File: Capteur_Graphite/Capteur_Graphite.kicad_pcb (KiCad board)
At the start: 2 copper layers, 68.6 x 53.3 mm, 25 parts, among them J1 Power, J2 Digital/PWM, J3 Analog, J4 Digital/PWM, U1 LTC1050ACN8_PBF, U2 MCP41050

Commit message: Clear PCB
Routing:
- net 13: track 111.3 -> 0.00 mm
- net +5: track 95.2 -> 0.26 mm
- net /SCL/A5: track 81.7 -> 0.00 mm
- net A1: track 41.1 -> 0.00 mm
- net R2: track 30.6 -> 0.00 mm
- net GND: track 20.9 -> 0.79 mm
- net Net-(U1-OUT): track 18.1 -> 0.14 mm
- net Net-(U1-+IN): track 17.0 -> 0.00 mm
- net A0: track 7.29 -> 0.00 mm
- net P2: track 5.45 -> 0.00 mm
- net Net-(Capteur1-cn): track 5.20 -> 0.00 mm

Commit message: Schematique propre
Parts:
- removed Encodeur: ~, Ma_Lib_Empreinte_Projet_Capteur:Rotatoire
- added U6: ~, Ma_Lib_Empreinte_Projet_Capteur:Rotatoire, F.Cu at (156.4, 53.5)
- C1, C2: footprint Capacitor_THT:C_Disc_D3.0mm_W1.6mm_P2.50mm -> Capacitor_THT:C_Disc_D5.0mm_W2.5mm_P5.00mm
- C3, C4: footprint Capacitor_THT:C_Rect_L4.6mm_W2.0mm_P2.50mm_MKS02_FKP02 -> Capacitor_THT:C_Rect_L7.0mm_W4.5mm_P5.00mm
- R1: footprint Resistor_THT:R_Axial_DIN0204_L3.6mm_D1.6mm_P7.62mm_Horizontal -> Resistor_THT:R_Axial_DIN0309_L9.0mm_D3.2mm_P5.08mm_Vertical
- R3, R5, R6: footprint Resistor_THT:R_Axial_DIN0204_L3.6mm_D1.6mm_P1.90mm_Vertical -> Resistor_THT:R_Axial_DIN0309_L9.0mm_D3.2mm_P5.08mm_Vertical

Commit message: Fin de séance du 13 mars
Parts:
- moved Bluetooth1 36.4 mm to (131.2, 92.0)
- moved U2 36.1 mm to (131.6, 53.0), turned to 90 degrees
- moved Rsensor1 26.6 mm to (148.0, 66.4)
- moved U1 26.1 mm to (151.0, 88.0)
- moved C4 14.6 mm to (128.5, 76.5)
- moved R3 14.3 mm to (133.1, 71.5)
- moved C2 13.7 mm to (144.0, 71.5), turned to 180 degrees
- moved R6 12.3 mm to (144.1, 76.5)
- moved R1 8.62 mm to (122.0, 82.1)
- moved C3 7.07 mm to (153.0, 62.0), turned to 0 degrees
- moved C1 5.00 mm to (116.0, 77.0)
- moved Flex1 4.00 mm to (120.5, 97.5)
- moved Capteur1 3.80 mm to (102.0, 75.8)
- moved R5 3.50 mm to (107.4, 77.0)
- moved U6 2.09 mm to (155.0, 55.0), turned to 180 degrees
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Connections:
- J1 pad 5: +5V -> +5
- J2 pad 1: /SCL/A5 -> SCL
- J2 pad 2: /SDA/A4 -> SDA
- J2 pad 7: /*11 -> 11
- J2 pad 8: /*10 -> 10
- J2 pad 9: /*9 -> ServoOut
- J3 pad 5: /SDA/A4 -> SDA
- J3 pad 6: /SCL/A5 -> SCL
- J4 pad 3: /*5 -> P5
- J4 pad 4: /4 -> P4
- J4 pad 6: /2 -> P2

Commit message: PCB fini
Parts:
- moved Bluetooth1 38.8 mm to (142.8, 55.0)
- moved Rsensor1 27.7 mm to (153.5, 93.5)
- moved C2 21.7 mm to (149.5, 92.5)
- moved R6 12.3 mm to (148.6, 88.0)
- moved U1 11.5 mm to (139.6, 86.5)
- moved U2 10.4 mm to (125.0, 61.0), turned to -90 degrees
- moved C3 7.43 mm to (160.0, 59.5), turned to -90 degrees
- moved R3 6.36 mm to (137.6, 67.0)
- moved C4 6.02 mm to (133.0, 72.5)
- moved U6 3.54 mm to (158.5, 55.0)
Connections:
- Bluetooth1 pad 5: VCC -> +5
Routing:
- net +5: track 0.26 -> 155.9 mm
- net ServoOut: track 0.00 -> 38.1 mm
- net A1: track 0.00 -> 37.3 mm
- net R2: track 0.00 -> 26.3 mm
- net Net-(U1-OUT): track 0.00 -> 23.5 mm
- net Net-(U1-+IN): track 0.00 -> 22.4 mm
- net SCL: track 0.00 -> 18.4 mm
- net 13: track 0.00 -> 15.6 mm
- net SDA: track 0.00 -> 14.8 mm
- net P2: track 0.00 -> 13.9 mm
- net P5: track 0.00 -> 12.7 mm
- net A0: track 0.00 -> 10.4 mm
- net P4: track 0.00 -> 10.1 mm
- net 11: track 0.00 -> 8.27 mm
- net TX: track 0.00 -> 6.79 mm
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- added copper zone on F.Cu, net GND

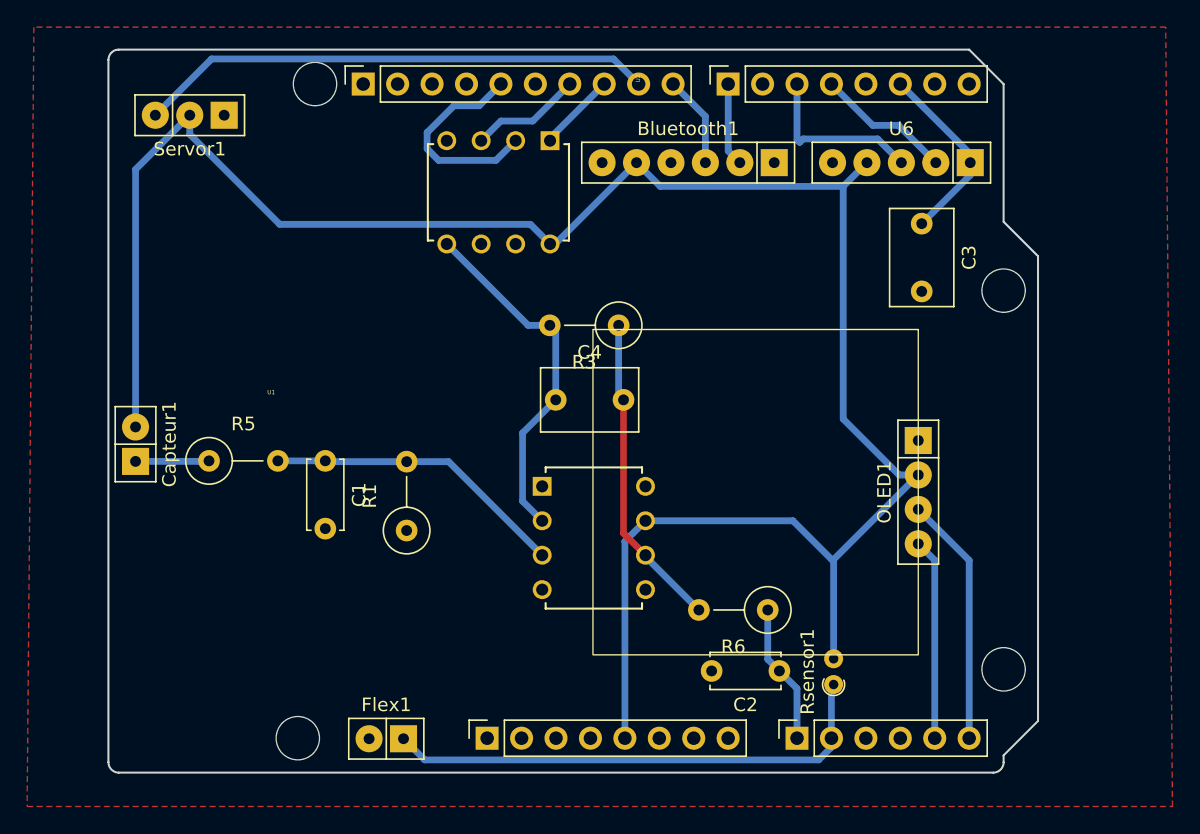
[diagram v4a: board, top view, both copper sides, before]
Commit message: ajout lib symbol + retouche kicad_pcb
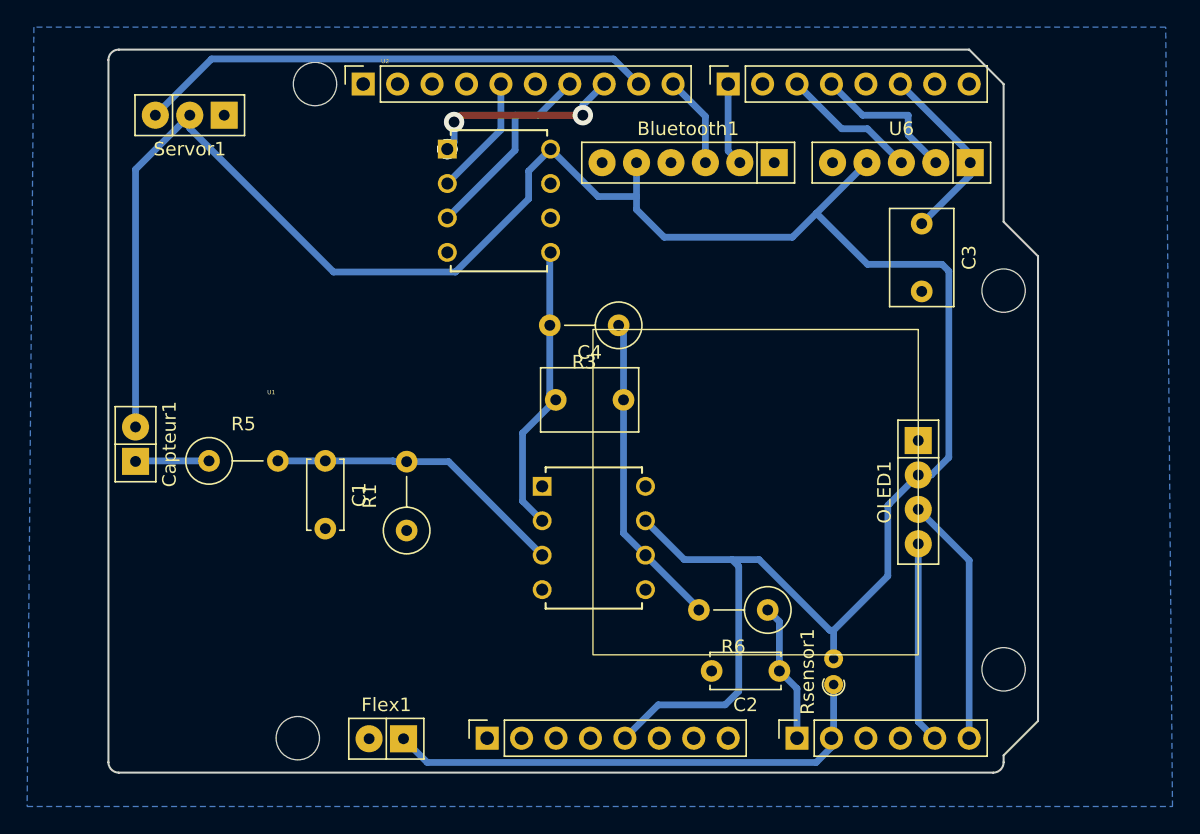
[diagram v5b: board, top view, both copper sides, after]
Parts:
- moved U2 7.69 mm to (132.6, 61.6), turned to 0 degrees
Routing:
- net +5: track 155.9 -> 174.2 mm
- net 10: track 5.84 -> 14.9 mm, vias 0 -> 4
- net 13: track 15.6 -> 8.98 mm
- net 11: track 8.27 -> 14.6 mm
- net R2: track 26.3 -> 21.6 mm
- net P5: track 12.7 -> 10.1 mm
- net P4: track 10.1 -> 11.0 mm
- net GND: track 0.79 -> 0.00 mm
- added copper zone on B.Cu, net GND
- removed copper zone on F.Cu, net GND

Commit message: Version Final du PCB + Gerber
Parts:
- Bluetooth1: footprint Ma_Lib_Empreinte_Projet_Capteur:HC05 -> Librairie empreinte:Bluetooth
- Capteur1: footprint Ma_Lib_Empreinte_Projet_Capteur:CapteurGraph -> Librairie empreinte:CapteurGraph
- Flex1: footprint Ma_Lib_Empreinte_Projet_Capteur:FlexSensor -> Librairie empreinte:FlexSensor
- OLED1: footprint Ma_Lib_Empreinte_Projet_Capteur:OLED -> Librairie empreinte:OLED
- Servor1: footprint Ma_Lib_Empreinte_Projet_Capteur:ServoMotor -> Librairie empreinte:ServoMotor
- U1, U2: footprint Ma_Lib_Empreinte_Projet_Capteur:LTC1050 -> Librairie empreinte:LTC1050
- U6: footprint Ma_Lib_Empreinte_Projet_Capteur:Rotatoire -> Librairie empreinte:Rotatoire
- moved U6 1.08 mm to (159.6, 55.0)
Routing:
- net +5: track 174.2 -> 180.2 mm
- net A1: track 37.5 -> 41.8 mm, vias 0 -> 2
- net P2: track 13.9 -> 15.2 mm
- net P5: track 10.1 -> 11.2 mm
- net 11: track 14.6 -> 13.6 mm

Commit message: Version Final corrigée du PCB
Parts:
- Rsensor1: footprint Resistor_THT:R_Axial_DIN0204_L3.6mm_D1.6mm_P1.90mm_Vertical -> Resistor_THT:R_Axial_DIN0309_L9.0mm_D3.2mm_P5.08mm_Vertical
- moved Rsensor1 1.45 mm to (154.0, 92.1)
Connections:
- Bluetooth1 pad 1: unconnected-(Bluetooth1-State-Pad1) -> GND
- Bluetooth1 pad 6: unconnected-(Bluetooth1-Key-Pad6) -> GND
- U1 pad 5: unconnected-(U1-EXTCLOCKINPUT-Pad5) -> GND
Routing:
- net A1: track 41.8 -> 5.59 mm, vias 2 -> 0
- net +5: track 180.2 -> 170.9 mm

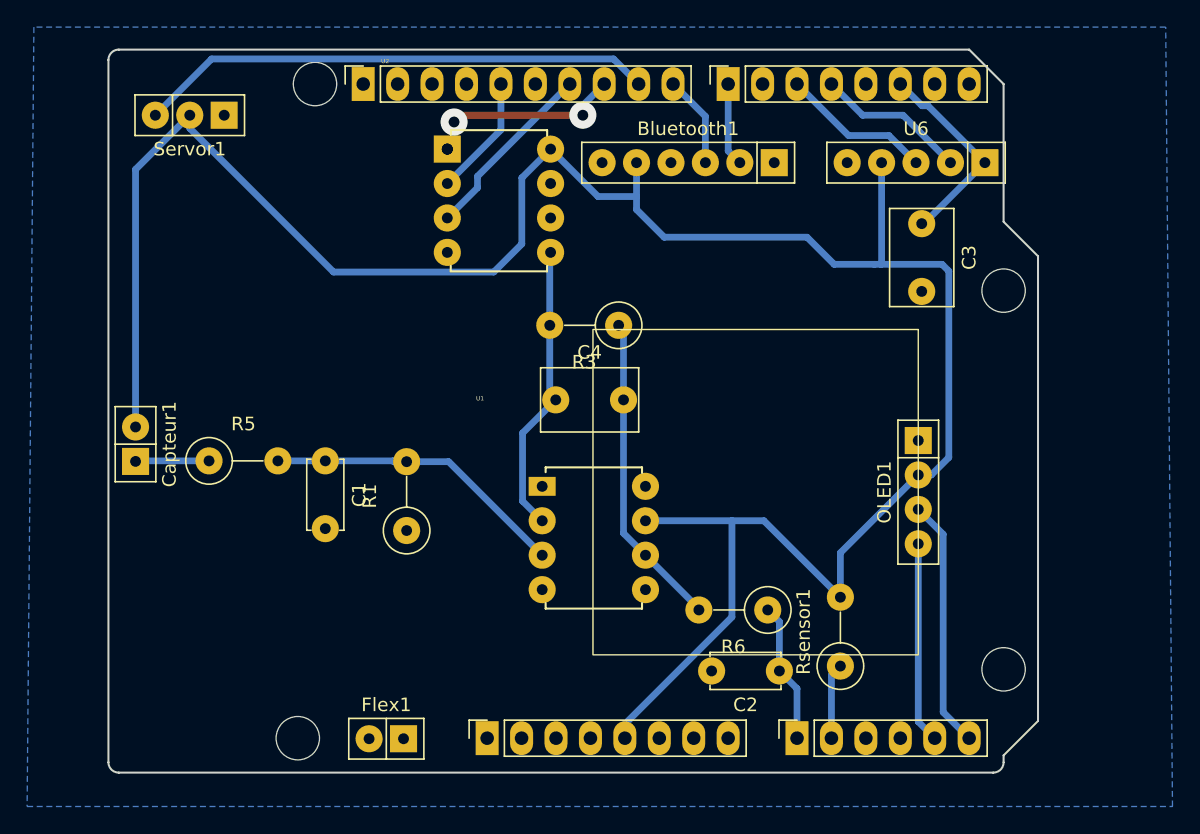
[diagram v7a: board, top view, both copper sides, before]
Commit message: Finale 3 GND connecté
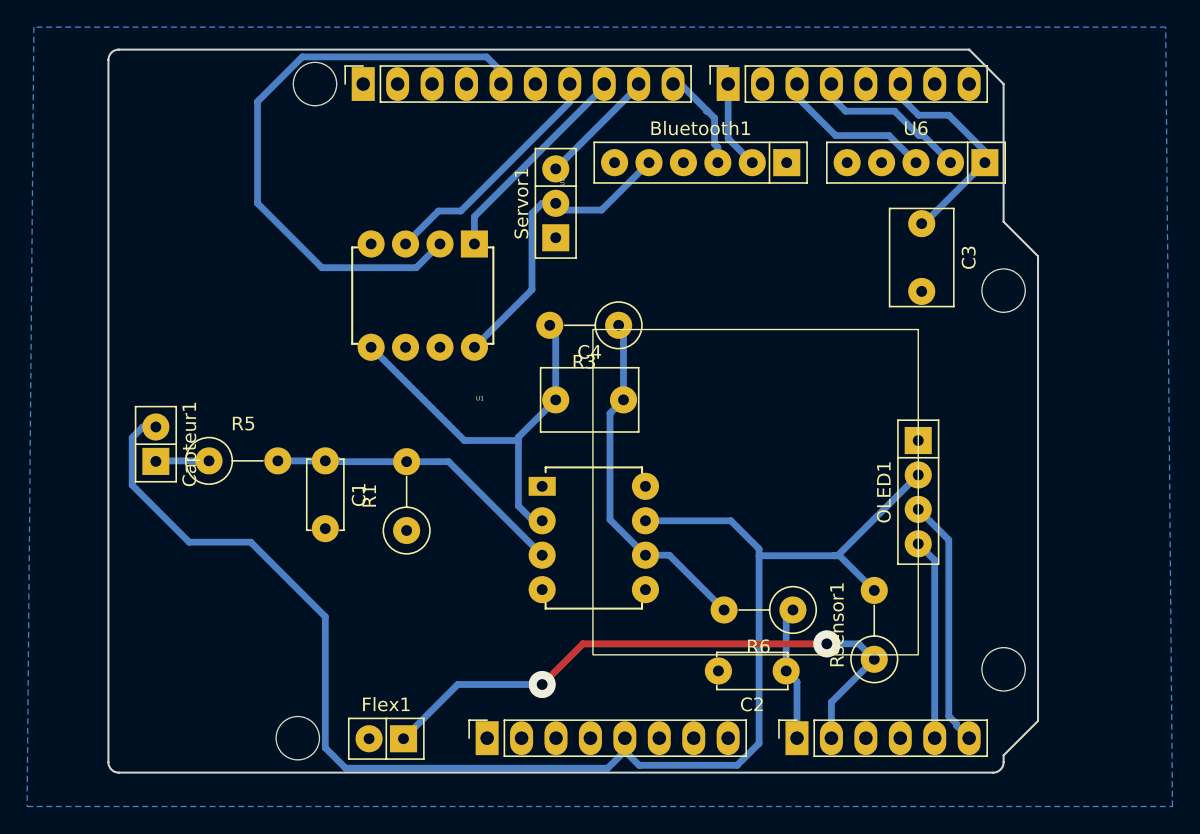
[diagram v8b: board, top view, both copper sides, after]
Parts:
- moved Servor1 27.8 mm to (133.0, 58.0), turned to -90 degrees
- moved U2 15.0 mm to (119.4, 68.6), turned to -90 degrees
- moved Rsensor1 2.55 mm to (156.5, 91.6)
- moved R6 1.86 mm to (150.5, 88.0)
- moved Capteur1 1.50 mm to (103.5, 75.8)
- moved Bluetooth1 0.92 mm to (143.7, 55.0)
- moved C2 0.50 mm to (150.0, 92.5)
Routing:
- net A1: track 5.59 -> 45.2 mm, vias 0 -> 2
- net +5: track 170.9 -> 132.8 mm
- net 13: track 8.98 -> 44.4 mm
- net ServoOut: track 38.1 -> 8.79 mm
- net R2: track 21.6 -> 30.6 mm
- net 11: track 13.6 -> 17.8 mm
- net Net-(U1-OUT): track 23.5 -> 26.1 mm
- net Net-(Capteur1-cn): track 5.44 -> 3.94 mm
- net P2: track 15.2 -> 16.2 mm
- net 10: track 14.9 -> 15.8 mm, vias 4 -> 0
- net TX: track 6.79 -> 7.54 mm
- net P5: track 11.2 -> 11.7 mm
- net P4: track 11.2 -> 11.7 mm
